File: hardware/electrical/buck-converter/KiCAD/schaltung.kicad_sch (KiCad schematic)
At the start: 19 parts, among them J1 V_in +, J10 GND, J2 V_in -, J3 V_OUT +, J4 V_OUT -, J5 PWM +, J6 I +, J7 U +, J8 GND, J9 GND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

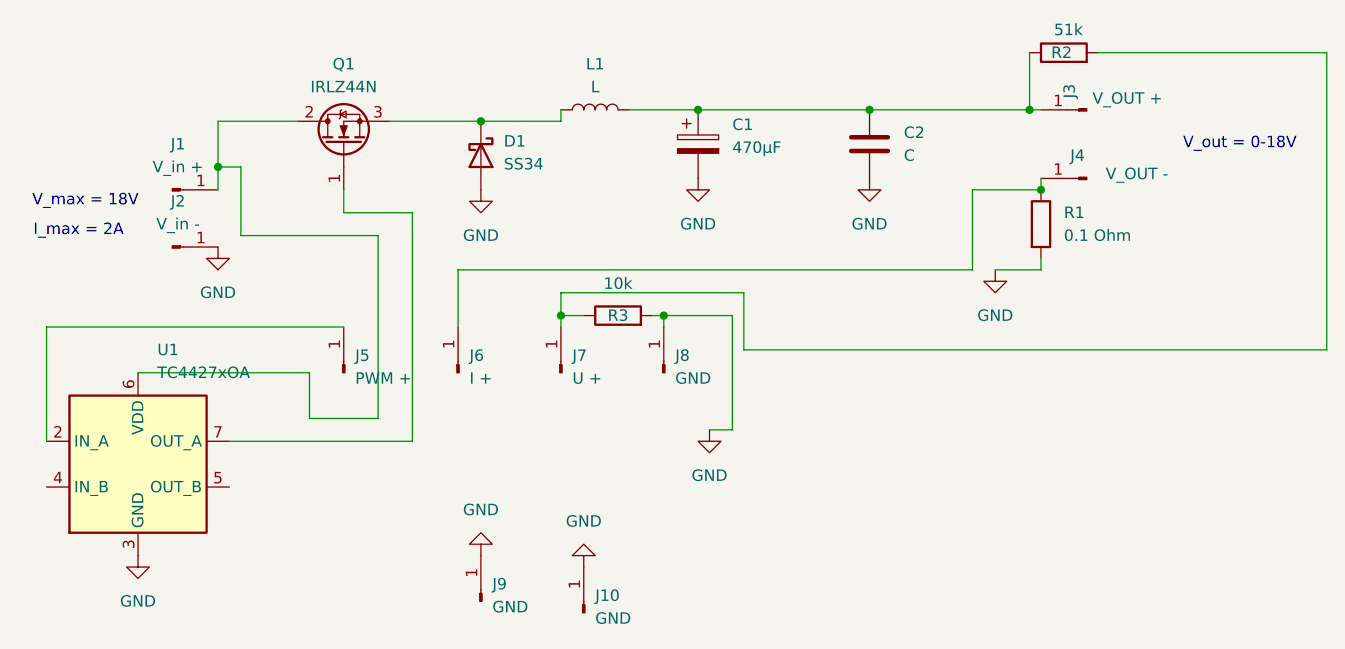
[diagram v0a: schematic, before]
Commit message: Updated PCBs; added Bleed Resistor and fixed Frontend GND connections
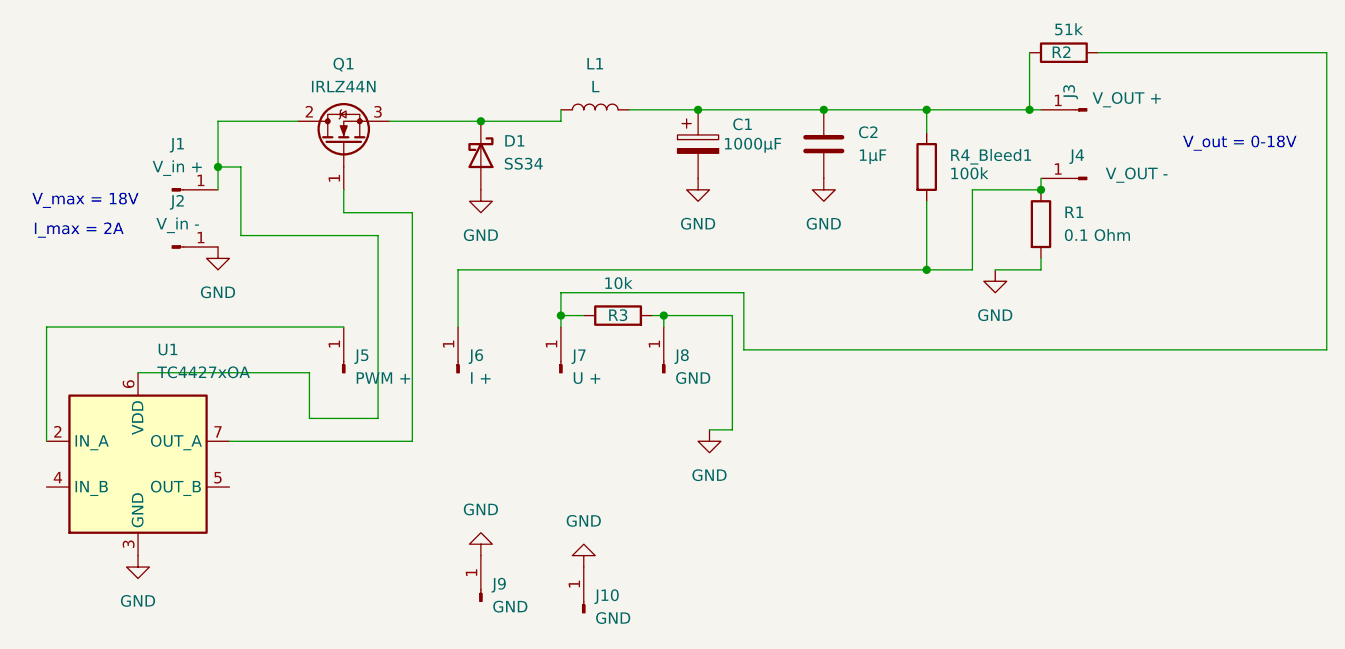
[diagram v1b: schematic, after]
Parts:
- added R4_Bleed1: 100k, Resistor_SMD:R_1206_3216Metric, symbol Device:R
- C1: value 470µF -> 1000µF
- C2: value C -> 1µF
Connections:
- net at C1.1, C2.1, J3.1 (Pin_1)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: now also R4_Bleed1.1
- net at J4.1 (Pin_1), J6.1 (Pin_1), R1.1: now also R4_Bleed1.2
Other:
- moved on the sheet: C2
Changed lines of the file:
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@@
+	)
+	(junction
+		(at 102.87 24.13)
+		(diameter 0)
+		(color 0 0 0 0)
 	)
 	(junction
@@
 	)
 	(junction
-		(at 107.95 24.13)
+		(at 114.3 41.91)
 		(diameter 0)
 		(color 0 0 0 0)
 	)
+	(junction
+		(at 114.3 24.13)
+		(diameter 0)
+		(color 0 0 0 0)
+	)
 	(wire
 		(pts
@@
 	(wire
 		(pts
-			(xy 107.95 24.13) (xy 125.73 24.13)
-		)
-		(stroke
-			(width 0)
-			(type default)
-		)
-	)
-	(wire
-		(pts
 			(xy 93.98 50.8) (xy 93.98 44.45)
 		)
@@
 	(wire
 		(pts
-			(xy 88.9 24.13) (xy 107.95 24.13)
+			(xy 88.9 24.13) (xy 102.87 24.13)
 		)
 		(stroke
@@
 	(wire
 		(pts
+			(xy 114.3 34.29) (xy 114.3 41.91)
+		)
+		(stroke
+			(width 0)
+			(type default)
+		)
+	)
+	(wire
+		(pts
 			(xy 73.66 46.99) (xy 73.66 48.26)
 		)
@@
 	(wire
 		(pts
+			(xy 102.87 24.13) (xy 114.3 24.13)
+		)
+		(stroke
+			(width 0)
+			(type default)
+		)
+	)
+	(wire
+		(pts
 			(xy 38.1 38.1) (xy 38.1 30.48)
 		)
@@
 	(wire
 		(pts
-			(xy 62.23 41.91) (xy 119.38 41.91)
+			(xy 114.3 24.13) (xy 125.73 24.13)
+		)
+		(stroke
+			(width 0)
+			(type default)
+		)
+	)
+	(wire
+		(pts
+			(xy 62.23 41.91) (xy 114.3 41.91)
 		)
 		(stroke
@@
 	(wire
 		(pts
+			(xy 114.3 26.67) (xy 114.3 24.13)
+		)
+		(stroke
+			(width 0)
+			(type default)
+		)
+	)
+	(wire
+		(pts
 			(xy 38.1 30.48) (xy 35.56 30.48)
+		)
+		(stroke
+			(width 0)
+			(type default)
+		)
+	)
+	(wire
+		(pts
+			(xy 114.3 41.91) (xy 119.38 41.91)
 		)
 		(stroke
@@
 		(on_board yes)
 		(dnp no)
-		(fields_autoplaced yes)
 		(property "Reference" "C1"
 			(at 92.71 25.7809 0)
@@
 			)
 		)
-		(property "Value" "470µF"
-			(at 92.71 28.3209 0)
+		(property "Value" "1000µF"
+			(at 91.694 27.94 0)
 			(effects
 				(font
@@
 	(symbol
 		(lib_id "Device:C")
-		(at 107.95 27.94 0)
-		(unit 1)
-		(exclude_from_sim no)
-		(in_bom yes)
-		(on_board yes)
-		(dnp no)
-		(fields_autoplaced yes)
+		(at 102.87 27.94 0)
+		(unit 1)
+		(exclude_from_sim no)
+		(in_bom yes)
+		(on_board yes)
+		(dnp no)
 		(property "Reference" "C2"
-			(at 111.76 26.6699 0)
+			(at 106.68 26.6699 0)
 			(effects
 				(font
@@
 			)
 		)
-		(property "Value" "C"
-			(at 111.76 29.2099 0)
+		(property "Value" "1µF"
+			(at 106.68 29.2099 0)
 			(effects
 				(font
@@
 		)
 		(property "Footprint" "Capacitor_THT:C_Disc_D5.0mm_W2.5mm_P5.00mm"
-			(at 108.9152 31.75 0)
+			(at 103.8352 31.75 0)
 			(effects
 				(font
@@
 		)
 		(property "Datasheet" "~"
-			(at 107.95 27.94 0)
+			(at 102.87 27.94 0)
 			(effects
 				(font
@@
 		)
 		(property "Description" "Unpolarized capacitor"
-			(at 107.95 27.94 0)
+			(at 102.87 27.94 0)
 			(effects
 				(font
@@
 	)
 	(symbol
+		(lib_id "Device:R")
+		(at 114.3 30.48 0)
+		(unit 1)
+		(exclude_from_sim no)
+		(in_bom yes)
+		(on_board yes)
+		(dnp no)
+		(property "Reference" "R4_Bleed1"
+			(at 116.84 29.2099 0)
+			(effects
+				(font
+					(size 1.27 1.27)
+				)
+				(justify left)
+			)
+		)
+		(property "Value" "100k"
+			(at 116.84 31.242 0)
+			(effects
+				(font
+					(size 1.27 1.27)
+				)
+				(justify left)
+			)
+		)
+		(property "Footprint" "Resistor_SMD:R_1206_3216Metric"
+			(at 112.522 30.48 90)
+			(effects
+				(font
+					(size 1.27 1.27)
+				)
+				(hide yes)
+			)
+		)
+		(property "Datasheet" "~"
+			(at 114.3 30.48 0)
+			(effects
+				(font
+					(size 1.27 1.27)
+				)
+				(hide yes)
+			)
+		)
+		(property "Description" "Resistor"
+			(at 114.3 30.48 0)
+			(effects
+				(font
+					(size 1.27 1.27)
+				)
+				(hide yes)
+			)
+		)
+		(pin "2"
+		)
+		(pin "1"
+		)
+		(instances
+			(project ""
+				(path "/54ae1450-4c93-4bd6-b065-173327891302"
+					(reference "R4_Bleed1")
+					(unit 1)
+				)
+			)
+		)
+	)
+	(symbol
 		(lib_id "Connector:Conn_01x01_Pin")
 		(at 62.23 53.34 90)
@@
 	(symbol
 		(lib_id "power:GND")
-		(at 107.95 31.75 0)
+		(at 102.87 31.75 0)
 		(unit 1)
 		(exclude_from_sim no)
@@
 		(fields_autoplaced yes)
 		(property "Reference" "#PWR06"
-			(at 107.95 38.1 0)
+			(at 102.87 38.1 0)
 			(effects
 				(font
@@
 		)
 		(property "Value" "GND"
-			(at 107.95 36.83 0)
+			(at 102.87 36.83 0)
 			(effects
 				(font
@@
 		)
 		(property "Footprint" ""
-			(at 107.95 31.75 0)
+			(at 102.87 31.75 0)
 			(effects
 				(font
@@
 		)
 		(property "Datasheet" ""
-			(at 107.95 31.75 0)
+			(at 102.87 31.75 0)
 			(effects
 				(font
@@
 		)
 		(property "Description" "Power symbol creates a global label with name \"GND\" , ground"
-			(at 107.95 31.75 0)
-			(effects
-				(font
+			(at 102.87 31.75 0)
+			(effects
+				(font
